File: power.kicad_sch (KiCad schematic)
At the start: 244 parts, among them J3 Conn_01x01, J4 Conn_01x01, U1 CSD95472Q5MC, U16 CSD95472Q5MC, U18 CSD95472Q5MC, U19 CSD95472Q5MC, U3 TPS53667, U36 MCP1824T-1202E, U4 CSD95472Q5MC, U5 CSD95472Q5MC, U6 AP3211, U7 MCP1824T-0802E

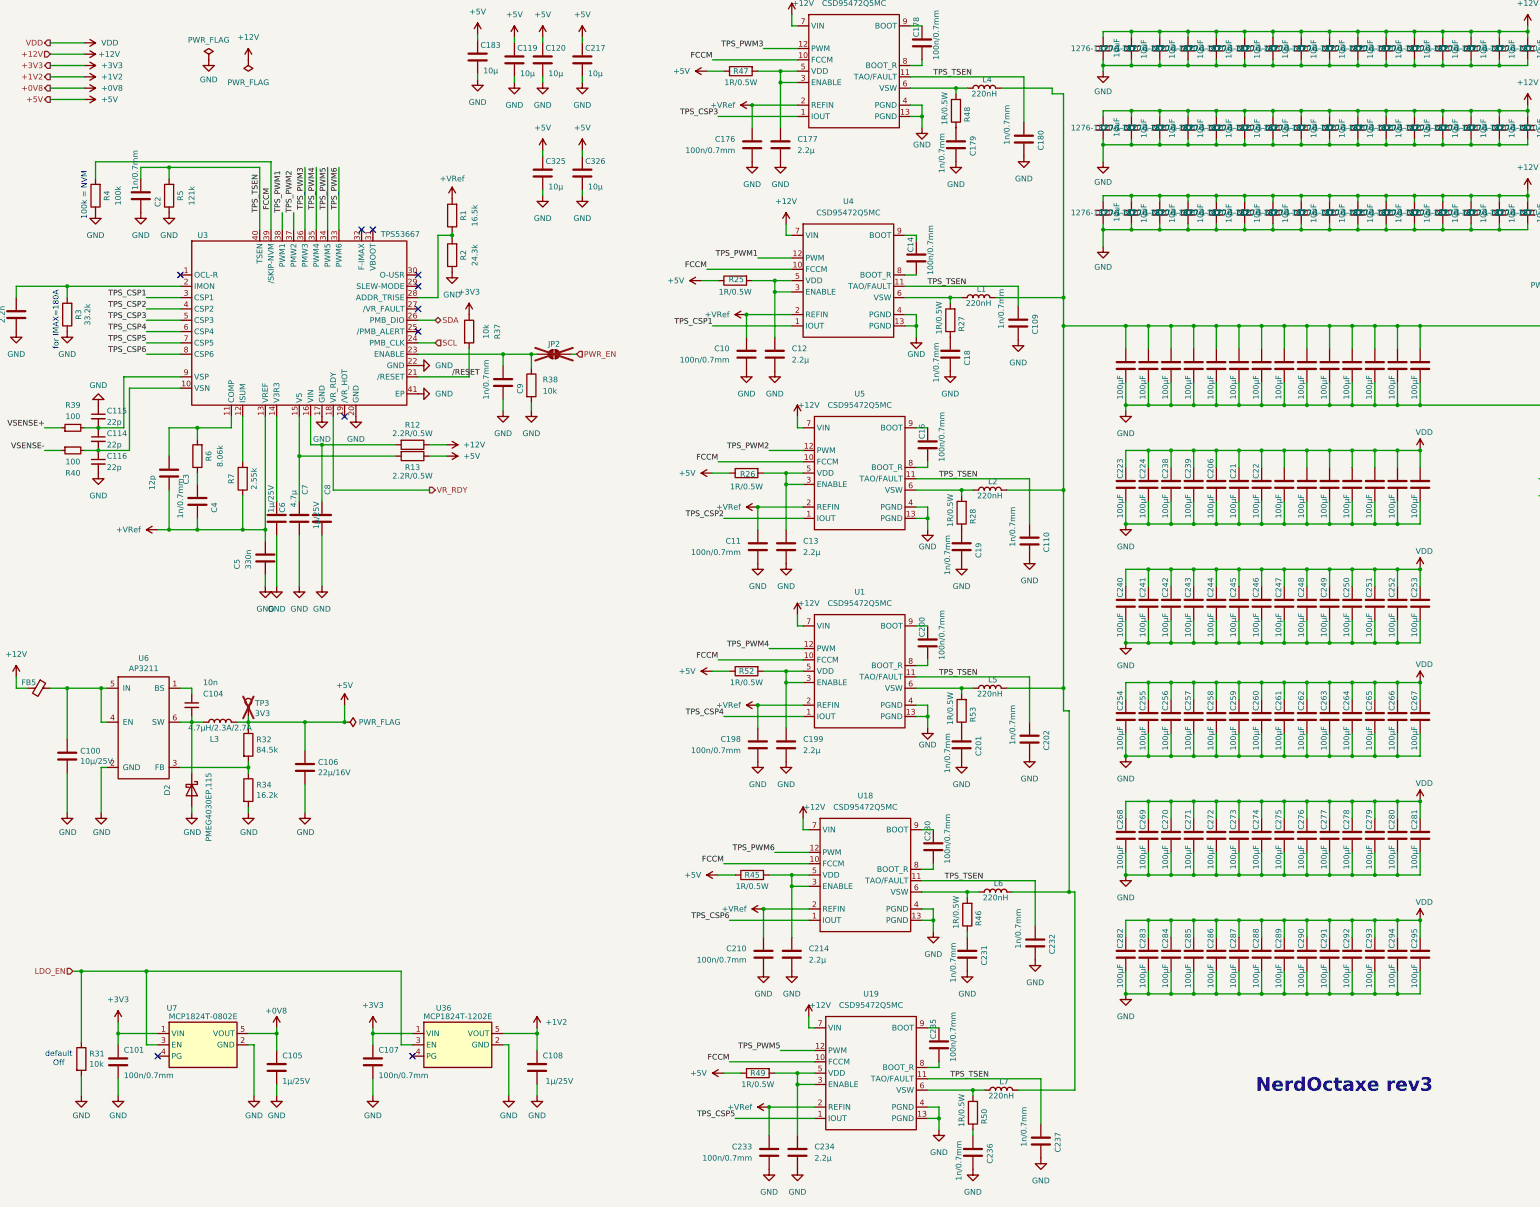
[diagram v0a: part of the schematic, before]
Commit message: Board Rev + Bom
Changes to R-C Values Snubber
BOM / iBOM / Partnumbers
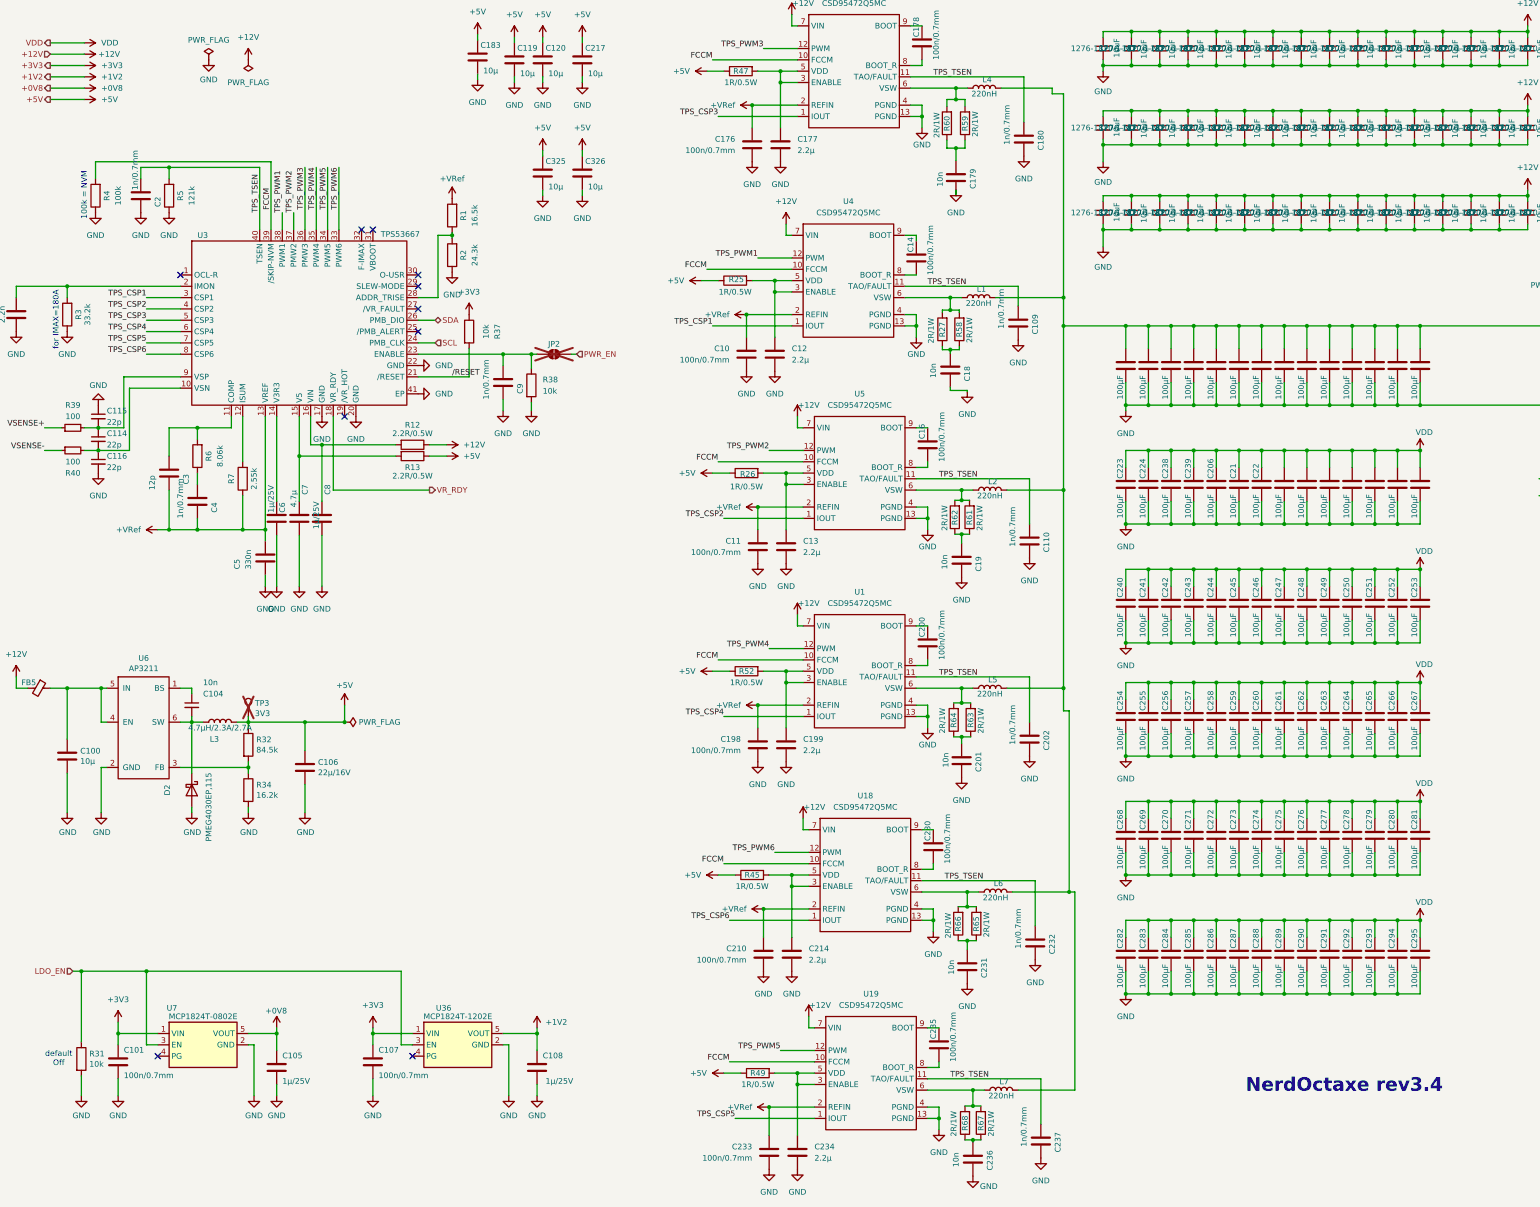
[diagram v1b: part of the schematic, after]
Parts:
- removed R28, R46, R48, R50, R53: 1R/0.5W, Resistor_SMD:R_0805_2012Metric, symbol Device:R
- added R58, R59, R60, R61, R62, R63, R64, R65, R66, R67, R68: 2R/1W, Resistor_SMD:R_1206_3216Metric, symbol Device:R
- C100: value 10µ/25V -> 10µ
- C104: LCSC C83170 -> (none); OrderNr 732-8021-1-ND -> 445-6947-1-ND
- C109, C110, C180, C2, C202, C232, C237, C4, C9: LCSC C1733 -> (none)
- C179, C18, C19, C201, C231, C236: value 1n/0.7mm -> 10n; LCSC C1733 -> (none); Manufacturer CC0805KRX7R0BB102 -> CGA4C2C0G1H103J060AA; OrderNr 311-1472-1-ND -> 445-6947-1-ND
- R27: value 1R/0.5W -> 2R/1W; footprint Resistor_SMD:R_0805_2012Metric -> Resistor_SMD:R_1206_3216Metric; LCSC C313850 -> (none); Manufacturer CRCW08051R00FKEAHP -> RCS12062R00FKEA; OrderNr 541-1.00TCT-ND -> 541-10616-1-ND
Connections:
- net at C201.1: now also R63.1, R64.1
- net at L5.1, U1.6 (VSW): now also R63.2, R64.2
- net at C179.1: now also R59.1, R60.1
- net at L4.1, U16.6 (VSW): now also R59.2, R60.2
- net at L7.1, U19.6 (VSW): now also R67.2, R68.2
- net at L6.1, U18.6 (VSW): now also R65.2, R66.2
- net at C236.1: now also R67.1, R68.1
- net at L2.1, U5.6 (VSW): now also R61.2, R62.2
- net at C18.1, R27.1: now also R58.1
- net at C19.1: now also R61.1, R62.1
- net at L1.1, R27.2, U4.6 (VSW): now also R58.2
- net at C231.1: now also R65.1, R66.1
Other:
- note added: "NerdOctaxe rev3.4"
- note removed: "NerdOctaxe rev3"
- moved on the sheet: C179, C18, C19, C201, C231, C236, R27

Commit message: Tmux Variant
- Added curcuit to read internal Asictemps per chip
- (i)BOM changes
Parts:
- C1: LCSC Part # (none) -> C1728
- C10, C101, C107, C11, C14, C16, C176, C178, C198, C200, C210, C230, C233, C235: LCSC Part # (none) -> C519981
- C100, C119, C120, C183, C217, C325, C326: LCSC Part # (none) -> C15850
- C104: LCSC Part # (none) -> C1845387; Manufacturer 885012207011 -> CGA4C2C0G1H103J060AA
- C105, C108, C6, C8: LCSC Part # (none) -> C116352
- C106: LCSC Part # (none) -> C159758
- C109, C110, C180, C2, C202, C232, C237, C4, C9: LCSC Part # (none) -> C162289; Manufacturer CC0805KRX7R0BB102 -> GRM2165C2A102JA01D; OrderNr 311-1472-1-ND -> 490-6445-1-ND
- C111, C112, C113, C117, C118, C181, C182, C191, C192, C20, C207, C209, C215, C216, C222, C23, C296, C297, C298, C299, C300, C301, C302, C303, C304, C305, C306, C307, C308, C309, C310, C311, C312, C313, C314, C315, C316, C317, C318, C319, C320, C321, C322, C323, C324, C45, C81, C89: LCSC Part # (none) -> C92487; Manufacturer (none) -> CL10A106MO8NQNC
- C114, C115, C116: LCSC Part # (none) -> C1653
- C12, C13, C177, C199, C214, C234: LCSC Part # (none) -> C87994
- C179, C18, C19, C201, C231, C236: LCSC Part # (none) -> C1845387
- C184, C185, C186, C187, C188, C189, C193, C194, C206, C21, C22, C223, C224, C238, C239, C24, C240, C241, C242, C243, C244, C245, C246, C247, C248, C249, C250, C251, C252, C253, C254, C255, C256, C257, C258, C259, C260, C261, C262, C263, C264, C265, C266, C267, C268, C269, C270, C271, C272, C273, C274, C275, C276, C277, C278, C279, C280, C281, C282, C283, C284, C285, C286, C287, C288, C289, C290, C291, C292, C293, C294, C295, C39, C48, C480, C481, C84, C86, C90, C91, C95, C97, C98, C99: LCSC Part # (none) -> C15008; Manufacturer (none) -> CL31A107MQHNNNE; OrderNr 399-C1210C107M8PAC7800CT-ND -> 1276-1782-1-ND
- C190, C208, C218, C92: LCSC Part # (none) -> C341198; Manufacturer 875075355002 -> HHXE250ARA221MHA0G
- C3: LCSC Part # (none) -> C1642
- C5: LCSC Part # (none) -> C161253
- C7: LCSC Part # (none) -> C1779
- D2: LCSC Part # (none) -> C96234
- FB5: LCSC Part # (none) -> C85840
- L1, L2, L4, L5, L6, L7: LCSC Part # (none) -> C2639748
- L3: LCSC Part # (none) -> C1331036
- R1: LCSC Part # (none) -> C35929
- R12, R13: LCSC Part # (none) -> C2078808
- R2: LCSC Part # (none) -> C101593
- R25, R26, R45, R47, R49, R52: LCSC Part # (none) -> C313850
- R27, R58, R59, R60, R61, R62, R63, R64, R65, R66, R67, R68: LCSC Part # (none) -> C4342787
- R29, R30: LCSC Part # (none) -> C17477
- R3: LCSC Part # (none) -> C4228823
- R31, R37, R38: LCSC Part # (none) -> C140868
- R32: LCSC Part # (none) -> C17842
- R34: LCSC Part # (none) -> C17481
- R39, R40: LCSC Part # (none) -> C17408
- R4: LCSC Part # (none) -> C96346
- R5: LCSC Part # (none) -> C17438
- R6: LCSC Part # (none) -> C2933501
- R7: LCSC Part # (none) -> C2933383
- U1, U16, U18, U19, U4, U5: LCSC Part # (none) -> C553137
- U3: LCSC Part # (none) -> C702270
- U36: LCSC Part # (none) -> C2971391
- U6: LCSC Part # (none) -> C154863
- U7: LCSC Part # (none) -> C625460

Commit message: minor monk stuff
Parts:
- added C329: 220µ/25V, Capacitor_SMD:CP_Elec_8x10, symbol Device:C_Polarized
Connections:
- net +12V: now also C329.1
- net GND: now also C329.2

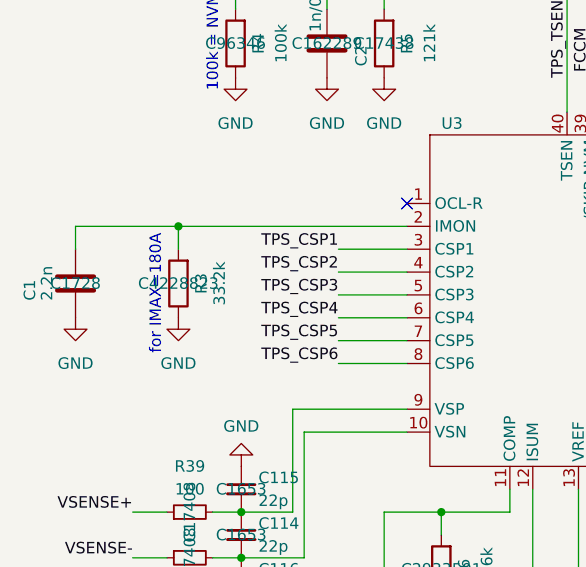
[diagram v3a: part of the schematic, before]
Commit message: BOM changes R3
changed 33.2k to 24.9k
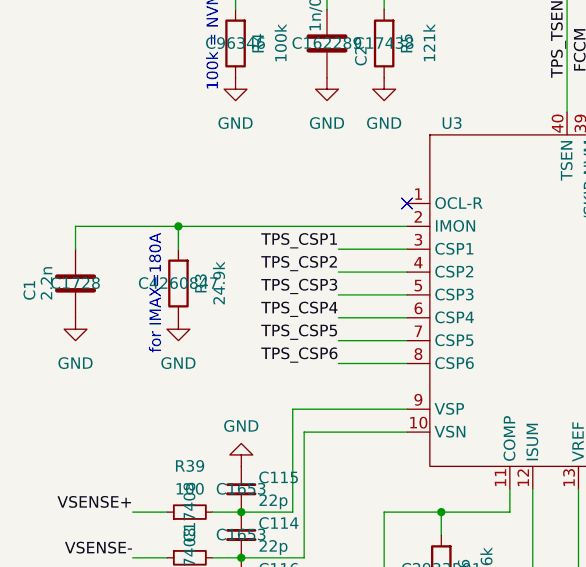
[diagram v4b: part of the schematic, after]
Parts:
- R3: value 33.2k -> 24.9k; LCSC Part # C4228823 -> C4260847; Manufacturer RMCF0805FT33K2 -> RMCF0805FT24K9; OrderNr RMCF0805FT33K2CT-ND -> RMCF0805FT24K9CT-ND
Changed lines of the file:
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@@
 			)
 		)
-		(property "Value" "33.2k"
+		(property "Value" "24.9k"
 			(at 40.132 87.63 90)
 			(effects
@@
 			)
 		)
-		(property "Description" "RES 33.2K OHM 1% 1/8W 0805"
+		(property "Description" "RES 24.9K OHM 1% 1/8W 0805"
 			(at 35.56 87.63 0)
 			(effects
@@
 			)
 		)
-		(property "OrderNr" "RMCF0805FT33K2CT-ND"
+		(property "OrderNr" "RMCF0805FT24K9CT-ND"
 			(at 35.56 87.63 90)
 			(effects
@@
 			)
 		)
-		(property "Manufacturer" "RMCF0805FT33K2"
+		(property "Manufacturer" "RMCF0805FT24K9"
 			(at 35.56 87.63 0)
 			(effects
@@
 			)
 		)
-		(property "LCSC Part #" "C4228823"
+		(property "LCSC Part #" "C4260847"
 			(at 35.56 87.63 0)
 			(effects

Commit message: Rev3.4
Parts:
- C179, C18, C19, C201, C231, C236: value 10n -> 6.8n; LCSC Part # C1845387 -> C3905032; Manufacturer CGA4C2C0G1H103J060AA -> GRM2165C2A682JA01D; OrderNr 445-6947-1-ND -> 490-GRM2165C2A682JA01DCT-ND
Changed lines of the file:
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@@
 			)
 		)
-		(property "Value" "10n"
+		(property "Value" "6.8n"
 			(at 231.394 58.928 90)
 			(effects
@@
 			)
 		)
-		(property "Description" "CAP CER 10000PF 50V C0G 0805"
+		(property "Description" "CAP CER 6800PF 100V C0G/NP0 0805"
 			(at 234.95 56.896 0)
 			(effects
@@
 			)
 		)
-		(property "Manufacturer" "CGA4C2C0G1H103J060AA"
+		(property "Manufacturer" "GRM2165C2A682JA01D"
 			(at 234.95 56.896 0)
 			(effects
@@
 			)
 		)
-		(property "OrderNr" "445-6947-1-ND"
+		(property "OrderNr" "490-GRM2165C2A682JA01DCT-ND"
 			(at 234.95 56.896 0)
 			(effects
@@
 			)
 		)
-		(property "LCSC Part #" "C1845387"
+		(property "LCSC Part #" "C3905032"
 			(at 234.95 56.896 0)
 			(effects
@@
 			)
 		)
-		(property "Value" "10n"
+		(property "Value" "6.8n"
 			(at 234.95 278.892 90)
 			(effects
@@
 			)
 		)
-		(property "Description" "CAP CER 10000PF 50V C0G 0805"
+		(property "Description" "CAP CER 6800PF 100V C0G/NP0 0805"
 			(at 238.76 277.114 0)
 			(effects
@@
 			)
 		)
-		(property "Manufacturer" "CGA4C2C0G1H103J060AA"
+		(property "Manufacturer" "GRM2165C2A682JA01D"
 			(at 238.76 277.114 0)
 			(effects
@@
 			)
 		)
-		(property "OrderNr" "445-6947-1-ND"
+		(property "OrderNr" "490-GRM2165C2A682JA01DCT-ND"
 			(at 238.76 277.114 0)
 			(effects
@@
 			)
 		)
-		(property "LCSC Part #" "C1845387"
+		(property "LCSC Part #" "C3905032"
 			(at 238.76 277.114 0)
 			(effects
@@
 			)
 		)
-		(property "Value" "10n"
+		(property "Value" "6.8n"
 			(at 229.87 101.854 90)
 			(effects
@@
 			)
 		)
-		(property "Description" "CAP CER 10000PF 50V C0G 0805"
+		(property "Description" "CAP CER 6800PF 100V C0G/NP0 0805"
 			(at 233.68 100.076 0)
 			(effects
@@
 			)
 		)
-		(property "Manufacturer" "CGA4C2C0G1H103J060AA"
+		(property "Manufacturer" "GRM2165C2A682JA01D"
 			(at 233.68 100.076 0)
 			(effects
@@
 			)
 		)
-		(property "OrderNr" "445-6947-1-ND"
+		(property "OrderNr" "490-GRM2165C2A682JA01DCT-ND"
 			(at 233.68 100.076 0)
 			(effects
@@
 			)
 		)
-		(property "LCSC Part #" "C1845387"
+		(property "LCSC Part #" "C3905032"
 			(at 233.68 100.076 0)
 			(effects
@@
 			)
 		)
-		(property "Value" "10n"
+		(property "Value" "6.8n"
 			(at 232.41 144.78 90)
 			(effects
@@
 			)
 		)
-		(property "Description" "CAP CER 10000PF 50V C0G 0805"
+		(property "Description" "CAP CER 6800PF 100V C0G/NP0 0805"
 			(at 236.22 142.748 0)
 			(effects
@@
 			)
 		)
-		(property "Manufacturer" "CGA4C2C0G1H103J060AA"
+		(property "Manufacturer" "GRM2165C2A682JA01D"
 			(at 236.22 142.748 0)
 			(effects
@@
 			)
 		)
-		(property "OrderNr" "445-6947-1-ND"
+		(property "OrderNr" "490-GRM2165C2A682JA01DCT-ND"
 			(at 236.22 142.748 0)
 			(effects
@@
 			)
 		)
-		(property "LCSC Part #" "C1845387"
+		(property "LCSC Part #" "C3905032"
 			(at 236.22 142.748 0)
 			(effects
@@
 			)
 		)
-		(property "Value" "10n"
+		(property "Value" "6.8n"
 			(at 233.934 235.712 90)
 			(effects
@@
 			)
 		)
-		(property "Description" "CAP CER 10000PF 50V C0G 0805"
+		(property "Description" "CAP CER 6800PF 100V C0G/NP0 0805"
 			(at 237.49 233.934 0)
 			(effects
@@
 			)
 		)
-		(property "Manufacturer" "CGA4C2C0G1H103J060AA"
+		(property "Manufacturer" "GRM2165C2A682JA01D"
 			(at 237.49 233.934 0)
 			(effects
@@
 			)
 		)
-		(property "OrderNr" "445-6947-1-ND"
+		(property "OrderNr" "490-GRM2165C2A682JA01DCT-ND"
 			(at 237.49 233.934 0)
 			(effects
@@
 			)
 		)
-		(property "LCSC Part #" "C1845387"
+		(property "LCSC Part #" "C3905032"
 			(at 237.49 233.934 0)
 			(effects
@@
 			)
 		)
-		(property "Value" "10n"
+		(property "Value" "6.8n"
 			(at 232.664 189.23 90)
 			(effects
@@
 			)
 		)
-		(property "Description" "CAP CER 10000PF 50V C0G 0805"
+		(property "Description" "CAP CER 6800PF 100V C0G/NP0 0805"
 			(at 236.22 187.706 0)
 			(effects
@@
 			)
 		)
-		(property "Manufacturer" "CGA4C2C0G1H103J060AA"
+		(property "Manufacturer" "GRM2165C2A682JA01D"
 			(at 236.22 187.706 0)
 			(effects
@@
 			)
 		)
-		(property "OrderNr" "445-6947-1-ND"
+		(property "OrderNr" "490-GRM2165C2A682JA01DCT-ND"
 			(at 236.22 187.706 0)
 			(effects
@@
 			)
 		)
-		(property "LCSC Part #" "C1845387"
+		(property "LCSC Part #" "C3905032"
 			(at 236.22 187.706 0)
 			(effects

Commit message: BOM correction
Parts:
- U3: Manufacturer TPS53647RTAR -> TPS53667RTAR; OrderNr 296-51986-1-ND -> 296-44940-1-ND
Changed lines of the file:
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@@
 			)
 		)
-		(property "Manufacturer" "TPS53647RTAR"
+		(property "Manufacturer" "TPS53667RTAR"
 			(at 87.63 90.17 0)
 			(effects
@@
 			)
 		)
-		(property "OrderNr" "296-51986-1-ND"
+		(property "OrderNr" "296-44940-1-ND"
 			(at 87.63 90.17 0)
 			(effects
